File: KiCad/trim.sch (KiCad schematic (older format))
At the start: 31 parts

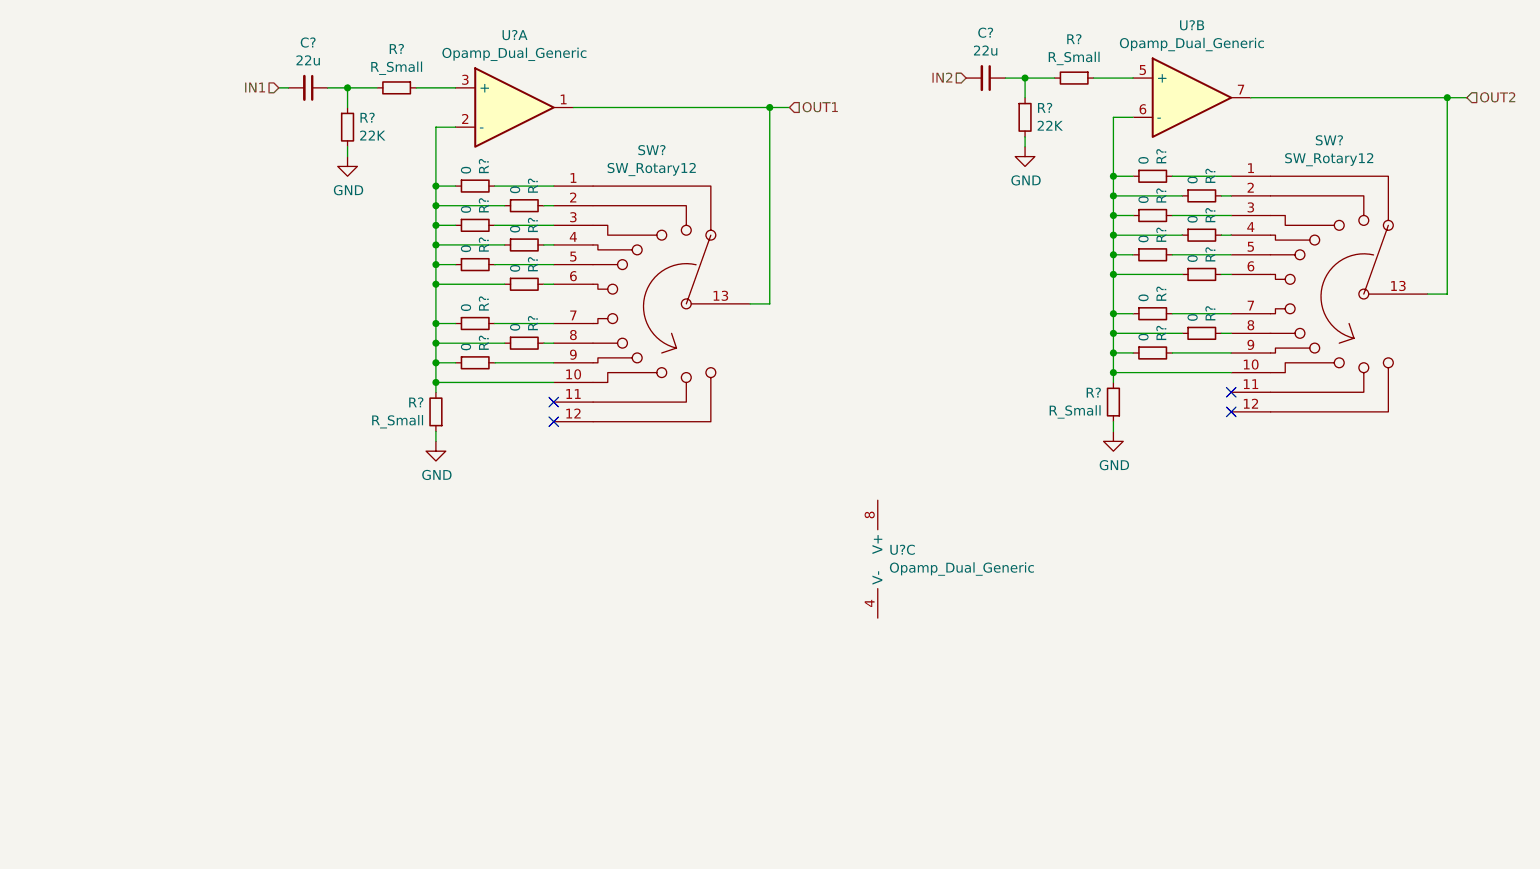
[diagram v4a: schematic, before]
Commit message: removed VU Meter sheet
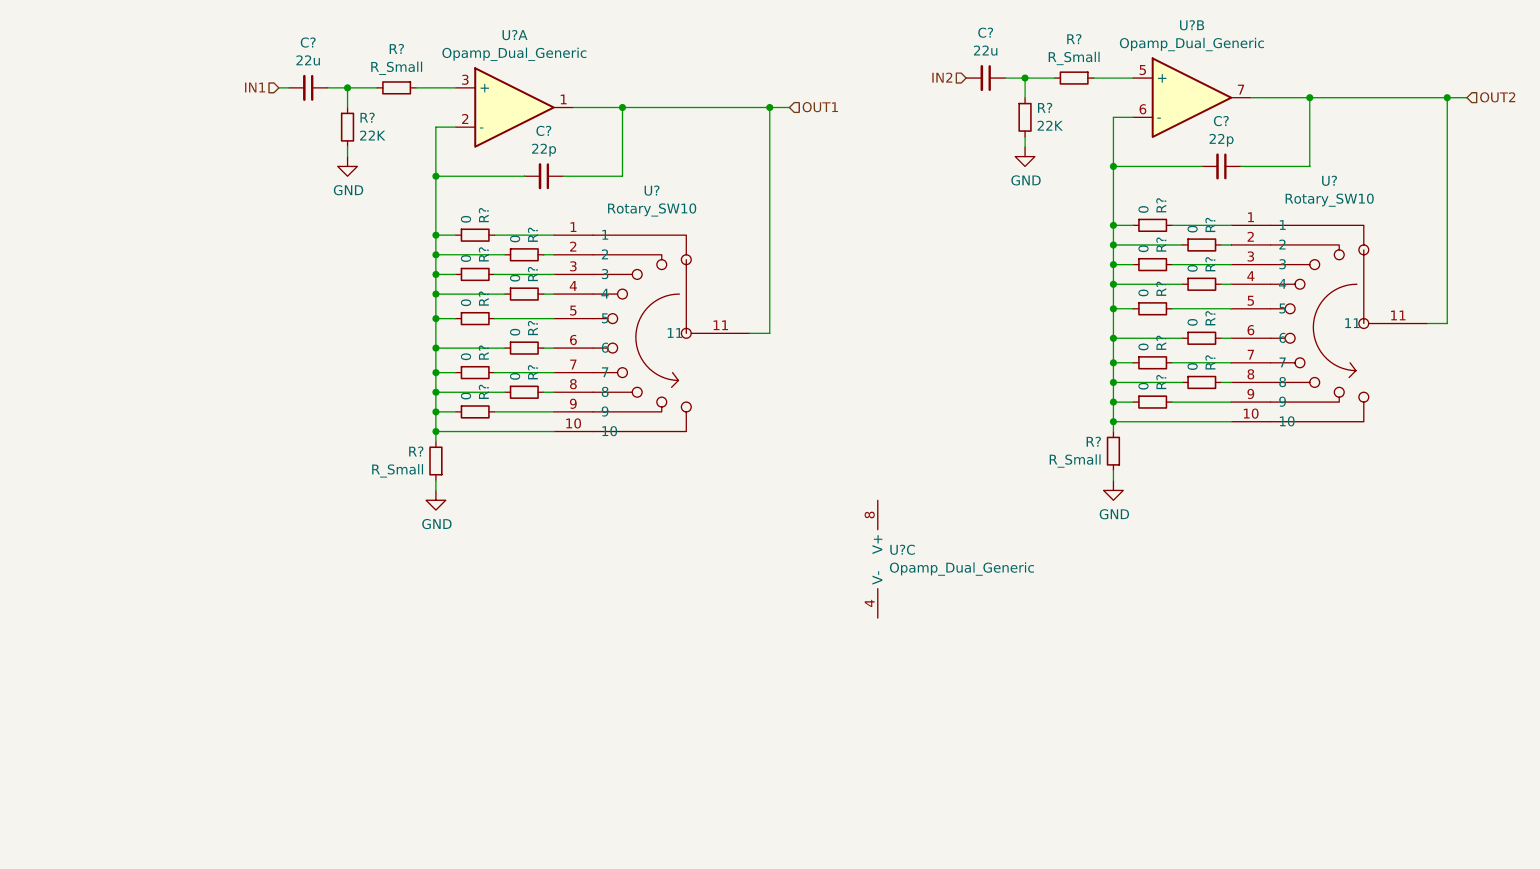
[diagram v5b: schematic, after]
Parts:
- removed R?: R_Small, symbol Device:R_Small
- removed R? (x9): 0, symbol Device:R_Small
- removed SW? (x2): SW_Rotary12, symbol Switch:SW_Rotary12
- added C? (x2): 22p, symbol Device:C_Small
- added R?: R_Small, symbol Device:R_Small
- added R? (x9): 0, symbol Device:R_Small
- added U? (x2): Rotary_SW10, symbol AmpModule:Rotary_SW10
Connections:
- net GND: now also R?.1
- net OUT1: now also C?.1, U?.11
- net OUT2: now also C?.1, U?.11
- net at R?.1, R?.1, R?.1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: now also C?.2, U?.10
- net at R?.2: now also U?.1
- net at R?.2: now also U?.2
- net at R?.2: now also U?.3
- net at R?.2: now also U?.4
- net at R?.2: now also U?.5
- net at R?.2: now also U?.6
- net at R?.2: now also U?.7
- net at R?.2: now also U?.8
- net at R?.2: now also U?.9
- net at U?.6 (-): now also C?.2, R?.1, R?.1, R?.1, R?.1, R?.1, R?.1, R?.1, R?.1, R?.1, R?.2, U?.10
- new net: R?.2, U?.9
- new net: R?.2, U?.8
- new net: R?.2, U?.7
- new net: R?.2, U?.6
- new net: R?.2, U?.5
- new net: R?.2, U?.4
- new net: R?.2, U?.3
- new net: R?.2, U?.2
- new net: R?.2, U?.1
- no-connect marks 4 -> 0
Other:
- moved on the sheet: R?
